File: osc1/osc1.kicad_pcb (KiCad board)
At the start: 2 copper layers, 50.4 x 131.5 mm, 60 parts, among them J1 LinFM, J10 PWMControl, J2 Hard Sync +, J3 Hard Sync -, J4 VOct, J5 Soft Sync Input, J6 Conn_02x08_Odd_Even, J7 Triangular Wave Output, J8 Square Wave Output, J9 Saw Wave Output, U1 AS3340, U2 TL072, U3 TL072

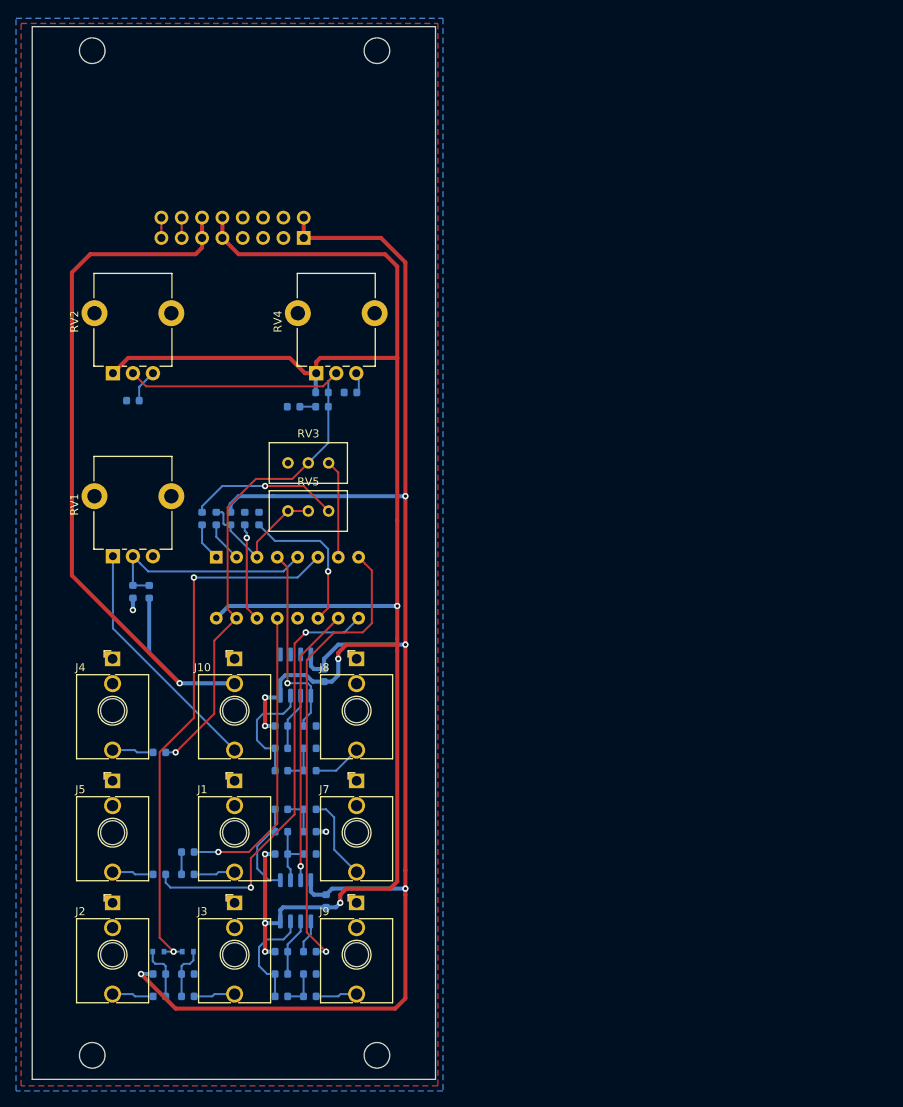
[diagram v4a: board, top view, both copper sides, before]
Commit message: osc1: all but hole diameters in frontplate done
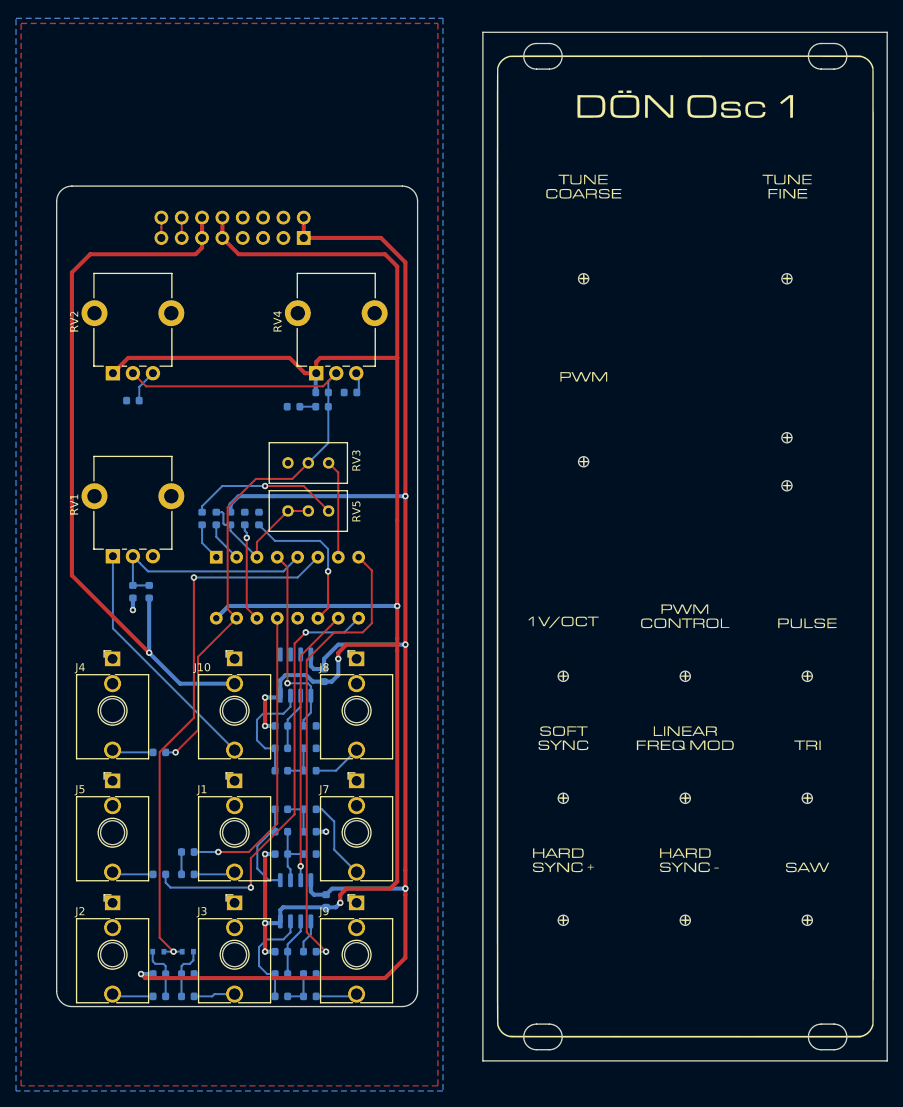
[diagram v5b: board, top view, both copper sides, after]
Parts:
- added G***: LOGO, osc1:frontplate, F.Cu at (150.3, 114.2)
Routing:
- net -12V: track 197.7 -> 191.5 mm
- net +5V: track 97.3 -> 91.9 mm
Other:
- board size 50.4 x 131.5 mm -> 103.7 x 128.5 mm
- board text added: "DÖN OSC1 rev 0"
- board text removed: "Note that the edge of this pcb should be made smaller so that it fits below the panel pcb!"

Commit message: osc1: extracted frontplate to a new project
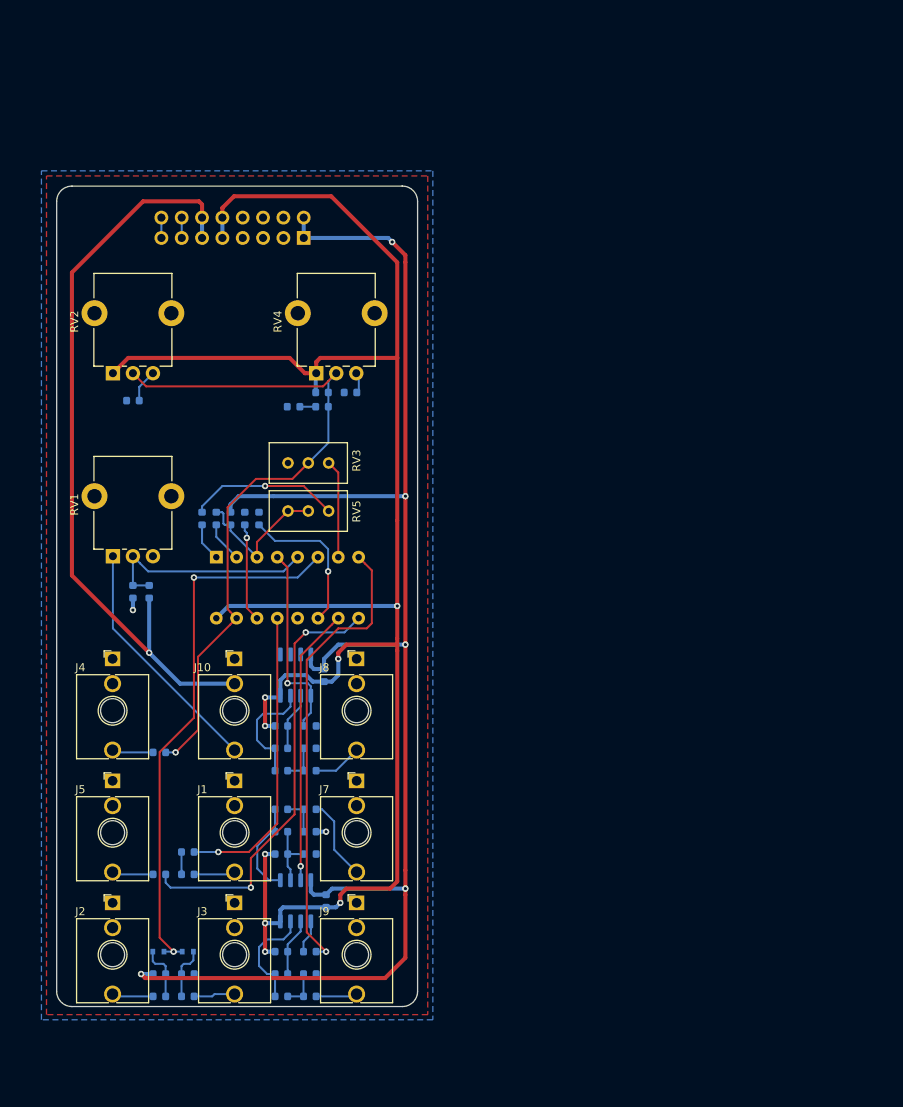
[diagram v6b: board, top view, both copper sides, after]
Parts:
- removed G***: LOGO, osc1:frontplate
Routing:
- net +12V: track 229.4 -> 233.7 mm
- net +5V: track 91.9 -> 94.9 mm
- net -12V: track 191.5 -> 192.1 mm, vias 4 -> 5
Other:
- board size 103.7 x 128.5 mm -> 45.1 x 102.5 mm

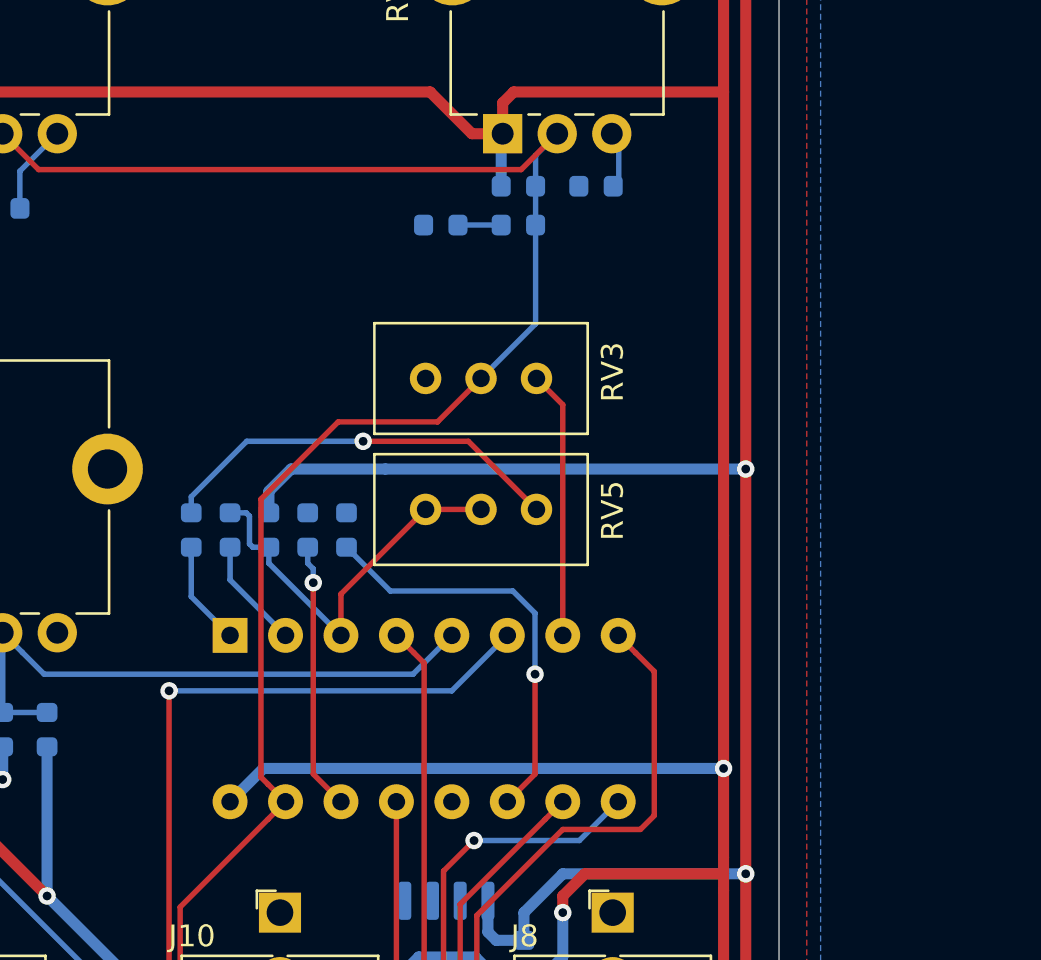
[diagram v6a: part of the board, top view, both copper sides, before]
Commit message: osc1: rev 0 fixes
Many minor fixes. Biggest change is adding a -5V LDO regulator.
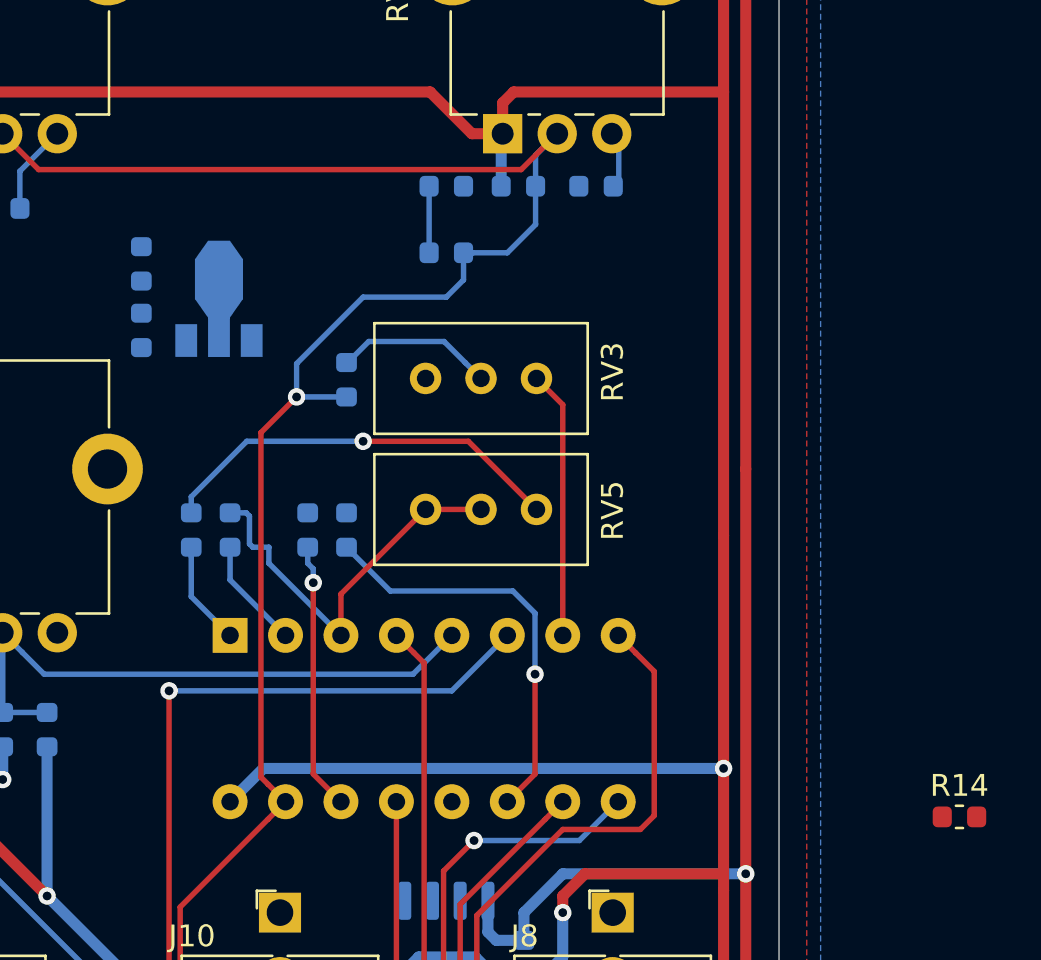
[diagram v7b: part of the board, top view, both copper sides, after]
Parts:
- added C10: 0.1u, Capacitor_SMD:C_0603_1608Metric, B.Cu at (87.6, 98.6)
- added C9: 0.1u, Capacitor_SMD:C_0603_1608Metric, B.Cu at (87.6, 101.6)
- added R33: 1M, Resistor_SMD:R_0603_1608Metric, B.Cu at (97.0, 103.9)
- added U4: L79L05_SOT89, Package_TO_SOT_SMD:SOT-89-3, B.Cu at (91.2, 100.6)
- R14: value 820 -> 1.5M; moved to F.Cu
- moved R14 34.3 mm to (125.1, 123.9), turned to 0 degrees
- moved R10 3.54 mm to (101.6, 98.0)
- moved C4 1.80 mm to (101.6, 95.0), turned to 180 degrees
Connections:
- J4 pad TN: Net-(J4-PadTN) -> (no net)
- J7 pad TN: Net-(J7-PadTN) -> (no net)
- J8 pad TN: Net-(J8-PadTN) -> (no net)
- J9 pad TN: Net-(J9-PadTN) -> (no net)
- R12 pad 2: Net-(R12-Pad2) -> Net-(C9-Pad1)
- R14 pad 1: Net-(R12-Pad2) -> LINFM
- R14 pad 2: -12V -> +12V
- RV3 pad 2: Net-(R10-Pad1) -> Net-(R33-Pad1)
- RV5 pad 2: Net-(R12-Pad2) -> Net-(C9-Pad1)
- RV5 pad 3: Net-(R12-Pad2) -> Net-(C9-Pad1)
- U1 pad 3: Net-(R12-Pad2) -> Net-(C9-Pad1)
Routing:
- net -12V: track 192.1 -> 168.8 mm, vias 5 -> 4
- net Net-(R12-Pad2): track 18.5 -> 0.00 mm
- net Net-(C9-Pad1): track 0.00 -> 18.5 mm
- net Net-(R33-Pad1): track 0.00 -> 7.26 mm
- net Net-(R10-Pad1): track 87.7 -> 90.7 mm, vias 1 -> 2
- net Net-(C4-Pad2): track 1.98 -> 3.05 mm
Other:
- board text added: "FIXME: The traces around R33/RV3/R10 are not pretty"

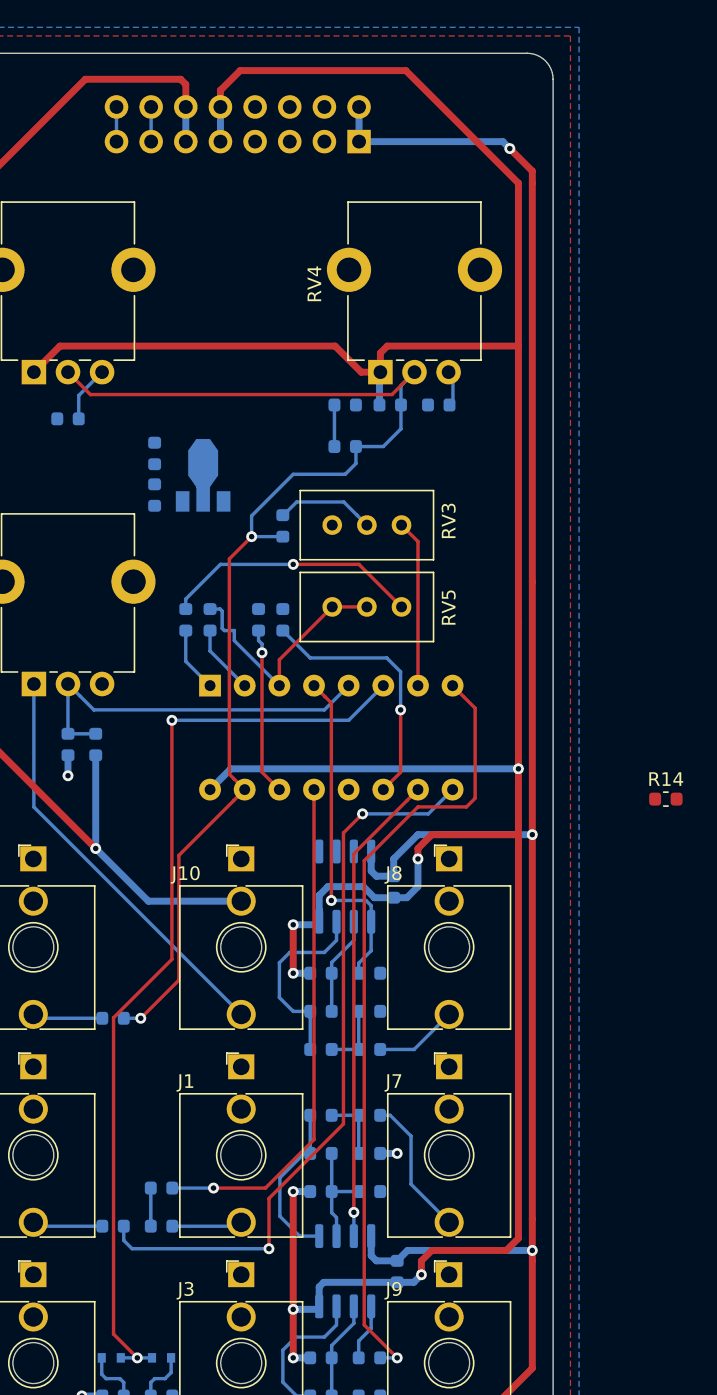
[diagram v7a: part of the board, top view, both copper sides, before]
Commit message: Add final fixes for rev 1
- 3D models for many parts
- Hysteresis between PWM and PULSOUT for better pulse shape (see datasheet)
- Fix a few resistor values that were unknown
- Layout of -5V regulator
- And more ...
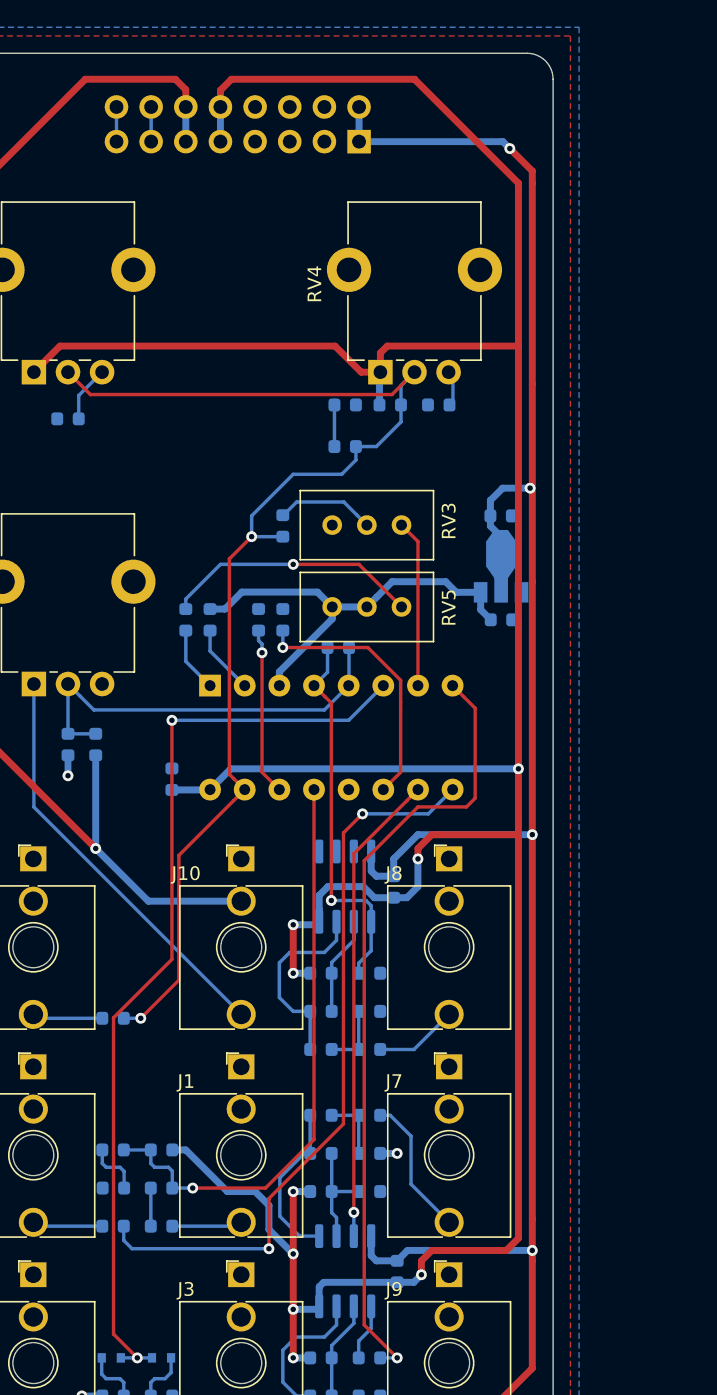
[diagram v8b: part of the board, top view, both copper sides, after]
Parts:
- added C11: 10n, Capacitor_SMD:C_0603_1608Metric, B.Cu at (84.6, 152.4)
- added C12: 0.1u, Capacitor_SMD:C_0603_1608Metric, B.Cu at (88.9, 122.4)
- added R34: 470, Resistor_SMD:R_0603_1608Metric, B.Cu at (84.6, 149.6)
- added R35: 1M, Resistor_SMD:R_0603_1608Metric, B.Cu at (101.1, 112.8)
- C10, C9: value 0.1u -> 1u
- R1: value 150k? -> 150k
- R14: moved to B.Cu
- R2, RV1: value 100k? -> 100k
- R7: value ? -> 220k
- R8: value ? -> 47k
- R9: value ? -> 1.5M
- RV2: value ? -> 10k
- RV4: value ? -> 100k
- moved R14 45.0 mm to (88.1, 149.6)
- moved C9 27.0 mm to (113.1, 110.7), turned to 0 degrees
- moved C10 25.8 mm to (113.0, 103.1), turned to 180 degrees
- moved U4 22.8 mm to (113.0, 107.3)
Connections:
- net Net-(C9-Pad1) renamed -5V
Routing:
- net +12V: track 233.7 -> 249.0 mm, vias 8 -> 9
- net -5V: track 18.5 -> 31.6 mm
- net -12V: track 168.8 -> 179.0 mm, vias 4 -> 5
- net LINFM: track 37.5 -> 43.5 mm
- net Net-(C11-Pad2): track 0.00 -> 4.05 mm
- net PULSOUT: track 24.7 -> 27.9 mm
- net PWMCTL: track 27.8 -> 30.6 mm
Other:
- board text added: "DÖN OSC1 rev 1"
- board text removed: "DÖN OSC1 rev 0"
- board text removed: "FIXME: The traces around R33/RV3/R10 are not pretty"
